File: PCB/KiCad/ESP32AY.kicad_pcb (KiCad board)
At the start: 2 copper layers, 55 x 100 mm, 109 parts, among them J1 ZX62D-B-5P8, J2 MiniJack, J3 SD Card, Q1 BC807, Q2 BC817, Q3 BC817, SW1 SW_Push, SW2 EN, SW3 BOOT, U1 AY-3-8910, U2 AY-3-8910, U3 CH340G, U4 ESP32-WROOM-32, U5 TPA6130A2RTJTG4, U6 SM5308, U7 AMS1117-3.3, U8 74HC595, U9 74HC595, Y3 12MHz

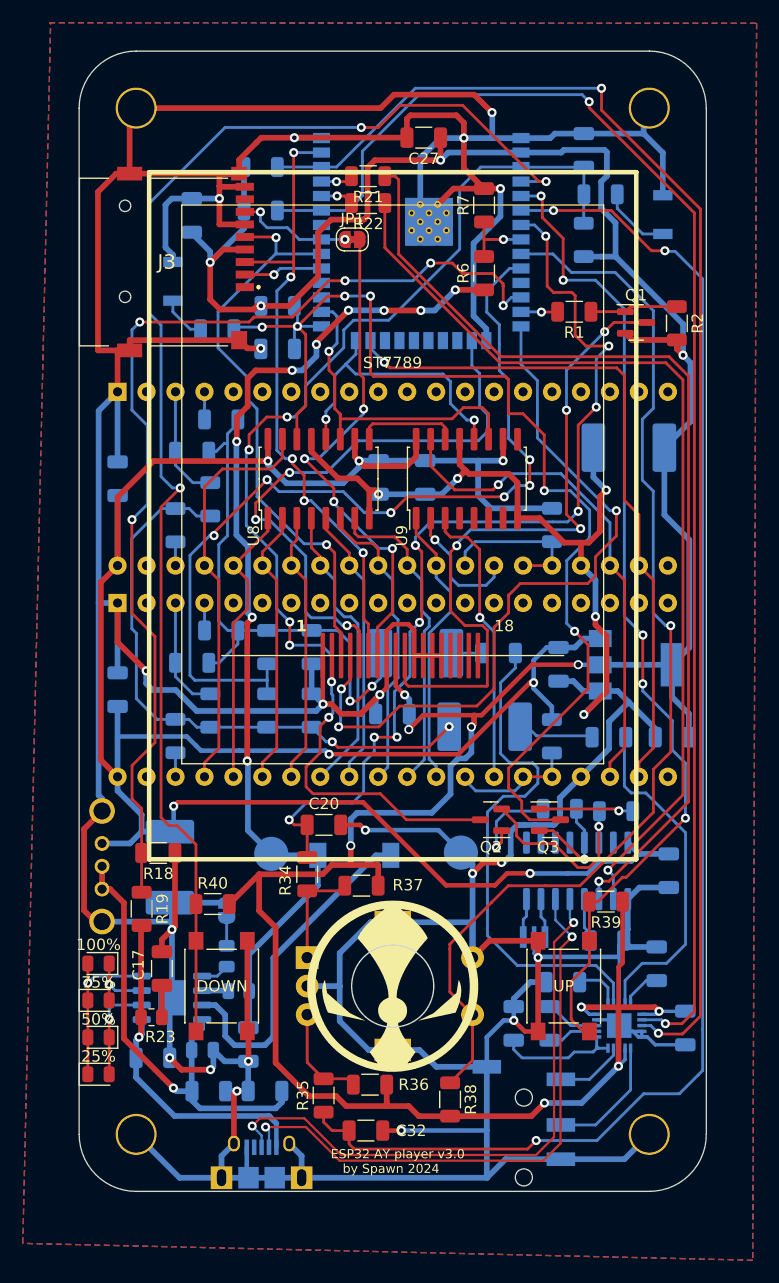
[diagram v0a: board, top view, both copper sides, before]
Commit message: Replaced miniUSB with typeC, changed small buttons, changed 12MHz crystal footprint
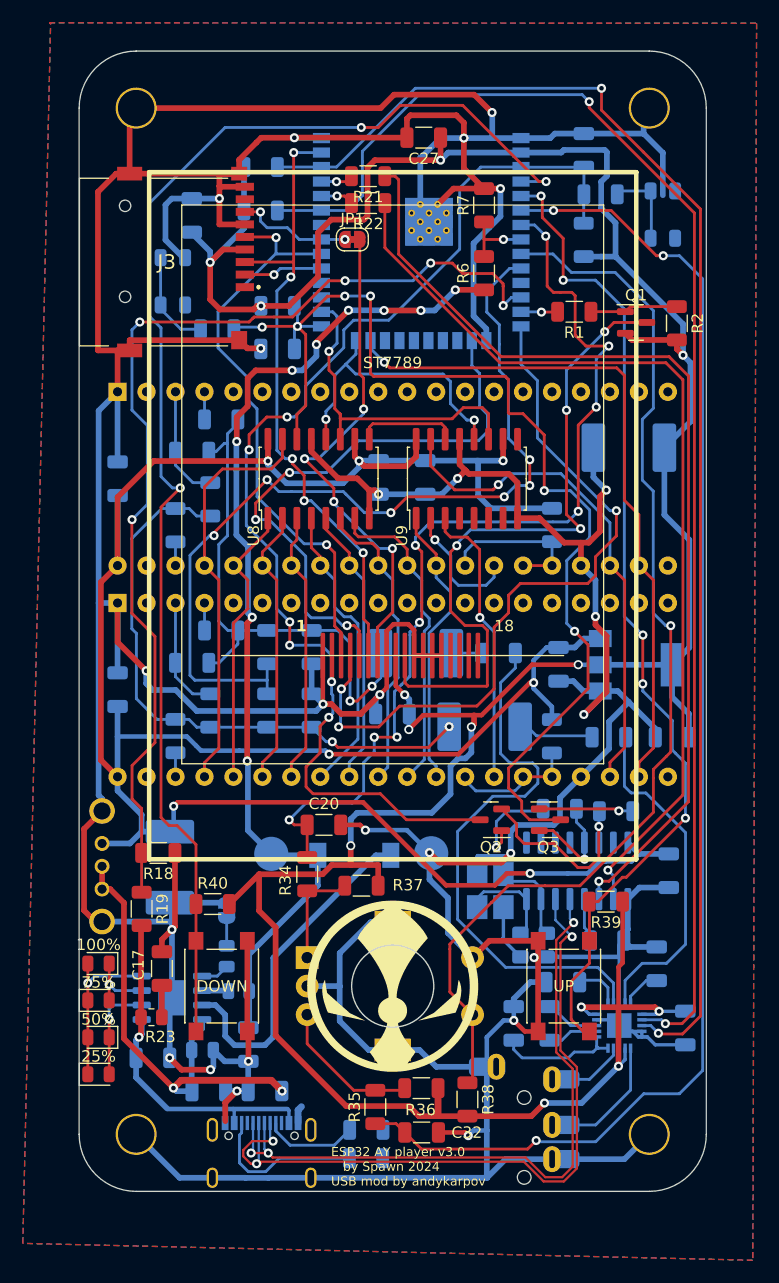
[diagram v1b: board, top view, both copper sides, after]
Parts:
- added C33: 22, Capacitor_SMD:C_0805_2012Metric_Pad1.18x1.45mm_HandSolder, B.Cu at (61.0, 98.4)
- added C34: 22, Capacitor_SMD:C_0805_2012Metric_Pad1.18x1.45mm_HandSolder, B.Cu at (58.7, 98.4)
- added R41: 5K1, Resistor_SMD:R_1206_3216Metric, B.Cu at (45.2, 114.6)
- added R42: 5K1, Resistor_SMD:R_1206_3216Metric, B.Cu at (45.2, 117.1)
- J1: value ZX62D-B-5P8 -> USB_C_Receptacle_USB2.0_14P; footprint mod:HRS_ZX62D-B-5P8 -> Connector_USB:USB_C_Receptacle_G-Switch_GT-USB-7010ASV
- J2: footprint mod:Jack_3.5mm_PJ320D_Horizontal -> footprints:AUDIO_JACK_3.5MM_SMD_TRRS_rounded_mixed
- R28, R30: value 470 -> 10K
- SW2, SW3: footprint Button_Switch_SMD:SW_SPST_B3U-1000P -> footprints:SW_SPST_PTS810_handsoldering
- Y3: footprint mod:OSC_CSTCE16M0V53-R0 -> Crystal:Crystal_SMD_3225-4Pin_3.2x2.5mm_HandSoldering
- moved J2 6.37 mm to (59.0, 120.4)
- moved Y3 5.60 mm to (56.1, 93.6), turned to -90 degrees
- moved C32 4.89 mm to (50.0, 114.8)
- moved R35 4.64 mm to (46.0, 112.6)
- moved R36 4.51 mm to (50.0, 110.9)
- moved BAT-1 2.60 mm to (50.9, 90.3)
- moved R38 1.52 mm to (54.1, 111.9)
- moved J1 1.00 mm to (36.0, 117.7)
- turned SW2 to 90 degrees
- turned SW3 to 90 degrees
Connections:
- Encoder1 pad MP: GND -> (no net)
- S6 pad P$4: GND -> (no net)
- S6 pad P$5: GND -> (no net)
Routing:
- net Net-(J1-CC2): track 0.00 -> 14.0 mm
- net GND: track 685.3 -> 671.5 mm
- net UD-: track 52.1 -> 65.5 mm, vias 2 -> 3
- net Net-(J1-CC1): track 0.00 -> 8.25 mm
- net UD+: track 52.6 -> 60.0 mm, vias 2 -> 3
- net ENC_B: track 126.5 -> 120.4 mm
- net Net-(U3-XO): track 3.45 -> 8.81 mm
- net Net-(SW3-B): track 4.04 -> 8.74 mm
- net Net-(U3-XI): track 3.47 -> 7.98 mm
- net Net-(Encoder1-PadB): track 9.04 -> 12.9 mm
- net Net-(U5-LEFTINP): track 45.3 -> 48.7 mm
- net Net-(SW2-B): track 6.17 -> 7.25 mm
- net Vin: track 31.2 -> 32.1 mm
- net +3.3V: track 286.7 -> 285.9 mm
- net ENC_OK: track 96.4 -> 95.8 mm
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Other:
- board text added: "ESP32 AY player v3.0 by Spawn 2024 USB mod by andykarpov"
- board text removed: "ESP32 AY player v3.0 by Spawn 2024"

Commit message: Replaced 1206 to 0805 hand soldering footprints
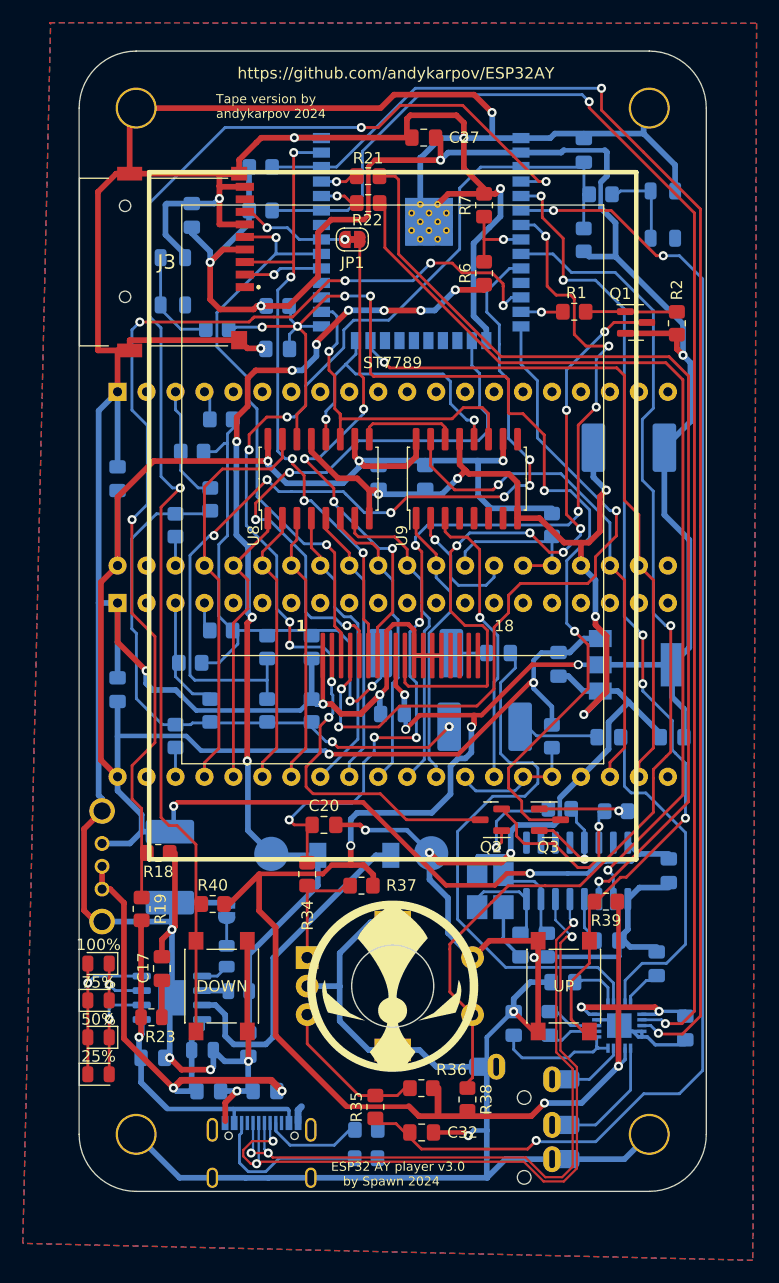
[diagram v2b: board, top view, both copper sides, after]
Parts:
- C1, C10, C11, C12, C13, C14, C16, C17, C18, C19, C2, C20, C21, C22, C24, C26, C27, C28, C29, C3, C30, C31, C32, C5, C6, C7, C8: footprint Capacitor_SMD:C_1206_3216Metric -> Capacitor_SMD:C_0805_2012Metric_Pad1.18x1.45mm_HandSolder
- R1, R10, R11, R12, R13, R14, R15, R16, R17, R18, R19, R2, R20, R21, R22, R26, R27, R28, R29, R3, R30, R31, R32, R33, R34, R35, R36, R37, R38, R39, R4, R40, R41, R42, R5, R6, R7, R8, R9: footprint Resistor_SMD:R_1206_3216Metric -> Resistor_SMD:R_0805_2012Metric_Pad1.20x1.40mm_HandSolder
- moved R15 0.17 mm to (29.7, 73.7)
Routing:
- net TFT_LED: track 59.3 -> 61.2 mm, vias 4 -> 6
- net ENC_A: track 85.6 -> 87.0 mm
- net AY1_A8: track 13.8 -> 14.5 mm
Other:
- board text added: "ESP32 AY player v3.0 by Spawn 2024"
- board text added: "Tape version by andykarpov 2024"
- board text added: "https://github.com/andykarpov/ESP32AY"
- board text removed: "ESP32 AY player v3.0 by Spawn 2024 USB mod by andykarpov"

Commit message: Changed tantalum cap footprints
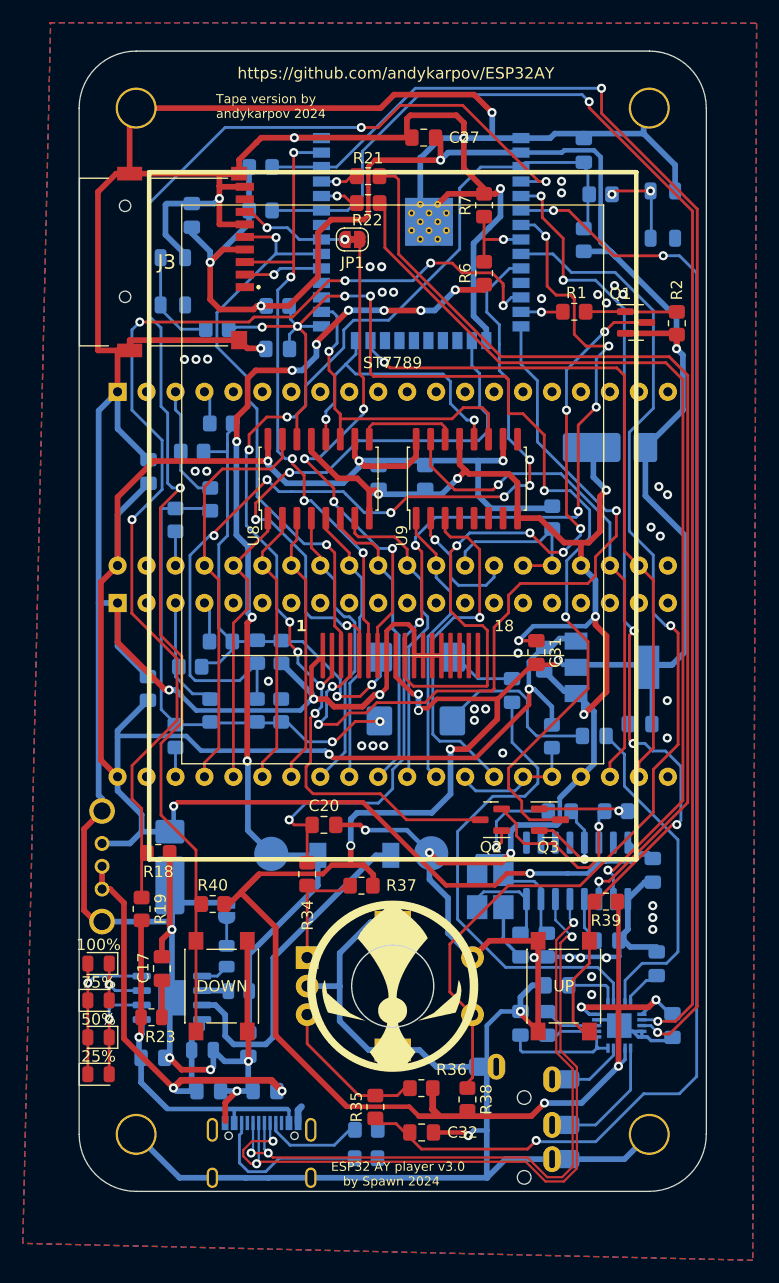
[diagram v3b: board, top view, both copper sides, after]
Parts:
- C15, C9: footprint Capacitor_Tantalum_SMD:CP_EIA-7360-38_Kemet-E -> Capacitor_Tantalum_SMD:CP_EIA-7343-31_Kemet-D_Pad2.25x2.55mm_HandSolder
- C25, C4: footprint Capacitor_Tantalum_SMD:CP_EIA-7360-38_Kemet-E -> footprints:CP_EIA-7343-31_Kemet-D-uni
- C31: moved to F.Cu
- moved C31 13.7 mm to (60.1, 72.7), turned to -90 degrees
- moved C15 6.05 mm to (49.5, 78.7)
- moved C13 3.49 mm to (58.0, 76.1), turned to 90 degrees
- moved C24 3.04 mm to (69.2, 79.0)
- moved C2 2.79 mm to (26.1, 56.9)
- moved R8 2.68 mm to (37.7, 72.7)
- moved R13 2.67 mm to (37.7, 77.8)
- moved C1 2.67 mm to (26.0, 75.9)
- moved U7 2.14 mm to (66.7, 74.0)
- moved C25 1.66 mm to (66.5, 54.8)
- moved C10 1.40 mm to (70.3, 91.8)
- moved C3 1.34 mm to (60.8, 73.3)
- moved C12 1.29 mm to (65.2, 80.1)
- moved C8 1.14 mm to (72.0, 105.5)
- moved R14 0.97 mm to (32.4, 71.8)
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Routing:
- net MIX_R: track 6.69 -> 15.7 mm
- net AYMIX_R: track 52.2 -> 43.4 mm
- net Net-(U5-LEFTINP): track 48.7 -> 42.3 mm
- net AY2_BDIR: track 25.6 -> 31.1 mm
- net MIX_L: track 2.67 -> 6.25 mm
- net TFT_DC: track 65.2 -> 67.9 mm
- net USB_SENS: track 92.0 -> 94.6 mm
- net AYMIX_L: track 47.6 -> 45.3 mm
- net +5V: track 214.1 -> 215.8 mm
- net +3.3V: track 285.7 -> 287.4 mm
- net ENC_OK: track 95.8 -> 97.3 mm
- net ENC_A: track 87.0 -> 85.6 mm, vias 9 -> 7
- net AY2_A: track 2.41 -> 3.57 mm
- net BT_DN: track 119.9 -> 121.0 mm
- net BT_UP: track 87.4 -> 88.5 mm
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
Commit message: Small silskreen fixes, moved tiny buttons on the one side
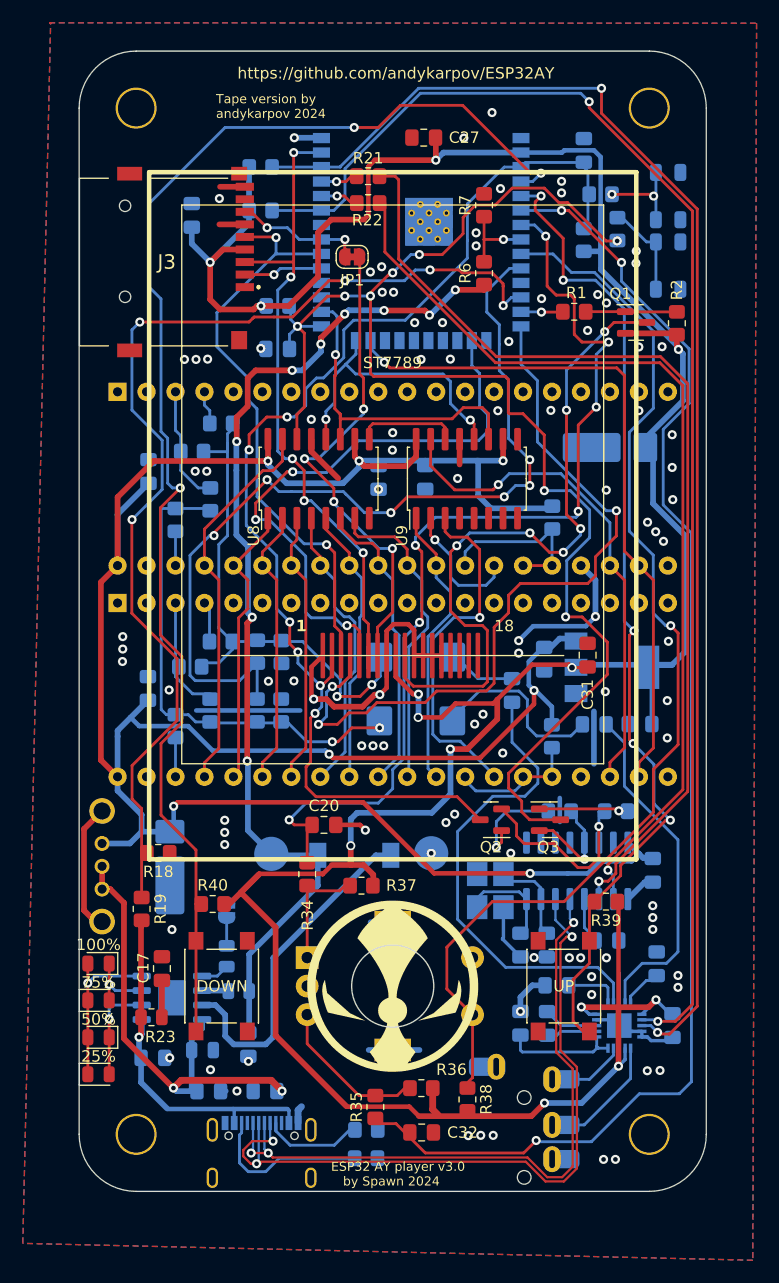
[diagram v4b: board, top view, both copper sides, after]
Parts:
- moved SW3 43.5 mm to (71.7, 38.8)
- moved R31 36.2 mm to (67.2, 35.6), turned to 90 degrees
- moved C31 4.50 mm to (64.6, 73.0)
- moved SW2 1.69 mm to (71.7, 32.7)
- moved JP1 1.53 mm to (43.9, 38.0)
- moved C12 1.02 mm to (65.2, 79.0)
- moved R17 0.87 mm to (28.4, 79.2)
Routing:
- net GND: track 670.7 -> 120.2 mm, vias 65 -> 100
- net 595_DATA: track 100.9 -> 125.9 mm, vias 6 -> 8
- net AY_D0: track 36.0 -> 34.0 mm
- net BT_UP: track 88.5 -> 86.8 mm
- net SPI_MISO: track 9.78 -> 11.3 mm
- net ENC_B: track 120.0 -> 118.4 mm
- net Net-(JP1-B): track 43.9 -> 42.4 mm
- net AY2_C: track 2.11 -> 3.44 mm
- net +5V: track 215.8 -> 214.6 mm
- net Net-(U5-RIGHTINP): track 29.2 -> 30.2 mm
- net BT_DN: track 121.0 -> 120.1 mm
- net ENC_OK: track 97.3 -> 96.4 mm
- net +3.3V: track 287.4 -> 288.1 mm
- net Net-(SW2-B): track 7.72 -> 8.39 mm
- net SDA: track 122.1 -> 121.5 mm
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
